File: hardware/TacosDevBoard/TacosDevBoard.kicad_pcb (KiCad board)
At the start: 2 copper layers, 63.6 x 108.1 mm, 12 parts, among them IC2_COMM1 Conn_01x08_Socket, J1 Conn_01x08_Socket, J2 Conn_01x08_Socket, J3 Conn_01x08_Socket, J4 Conn_01x08_Socket, J5 Conn_01x08_Socket, J6 Micro_SD_Card_Det2, J7 Conn_02x17_Counter_Clockwise, J9 Conn_01x10_Pin

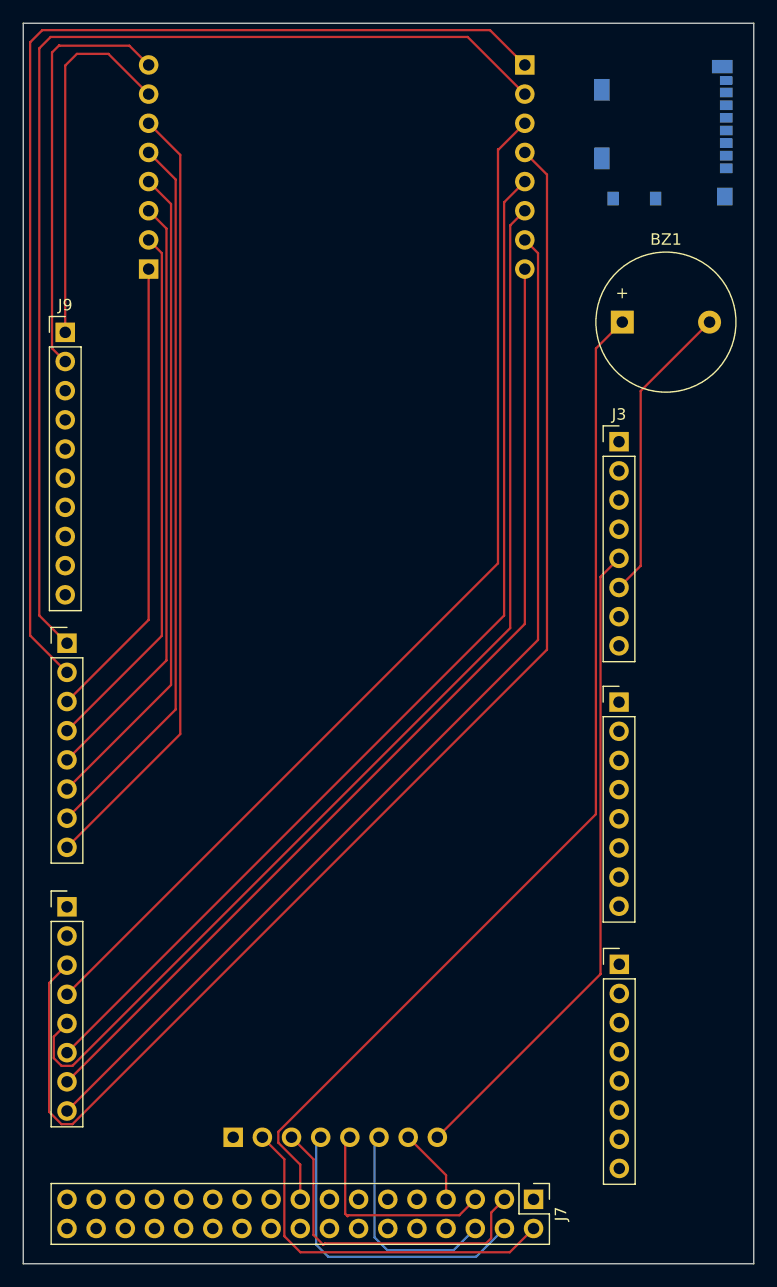
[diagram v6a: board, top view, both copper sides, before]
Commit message: added sd card to dev board
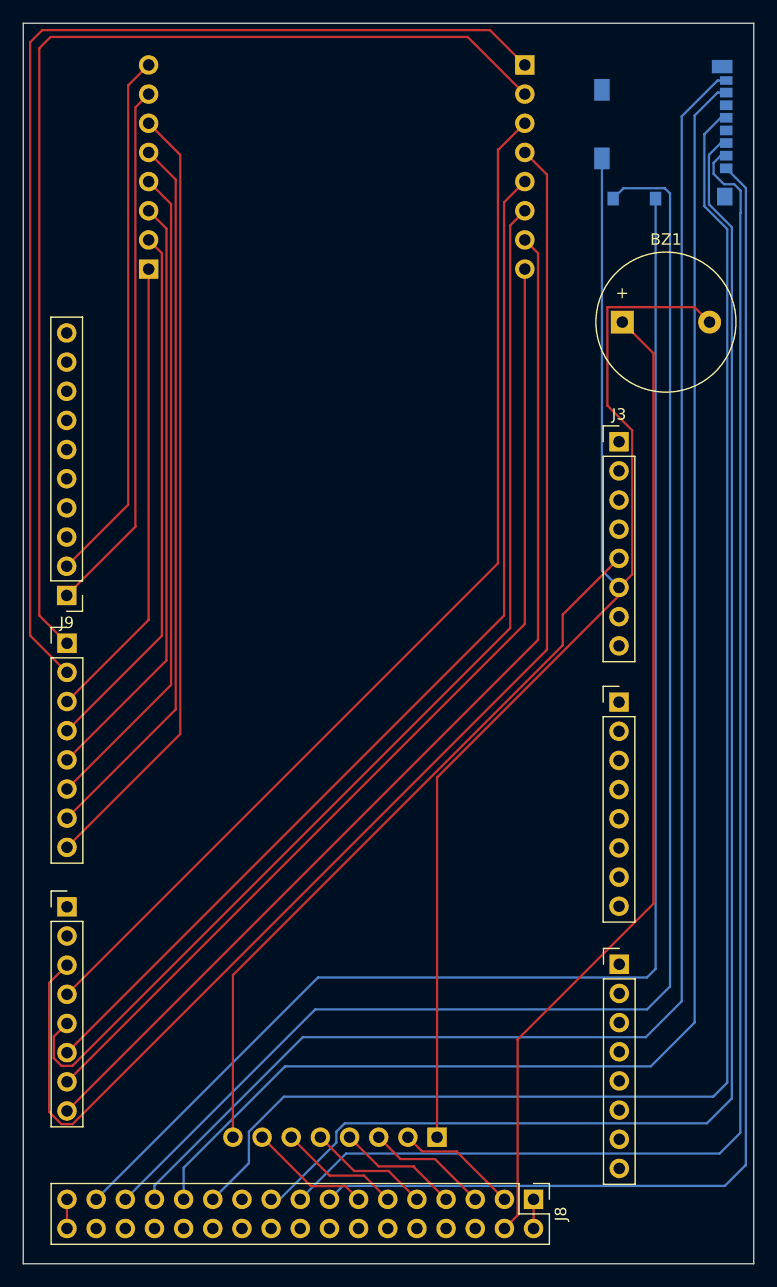
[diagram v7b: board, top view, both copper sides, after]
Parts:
- removed J7: Conn_02x17_Counter_Clockwise, Connector_PinHeader_2.54mm:PinHeader_2x17_P2.54mm_Vertical
- added J8: Conn_02x17_Odd_Even, Connector_PinHeader_2.54mm:PinHeader_2x17_P2.54mm_Vertical, F.Cu at (153.7, 136.9)
- moved J9 22.9 mm to (113.0, 84.3), turned to 180 degrees
- moved SELECT1 17.8 mm to (145.3, 131.5), turned to 90 degrees
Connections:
- J3 pad 4: +3.3V -> VDD
- J3 pad 7: GND -> VSS
- J6 pad 1: Net-(J6-DAT2) -> SD_DAT2
- J6 pad 10: Net-(J6-DET_A) -> SD_DET_A
- J6 pad 11: unconnected-(J6-SHIELD-Pad11) -> GND
- J6 pad 2: Net-(J6-DAT3/CD) -> SD_DAT3/CD
- J6 pad 3: Net-(J6-CMD) -> SD_CMD
- J6 pad 4: Net-(J6-VDD) -> VDD
- J6 pad 5: Net-(J6-CLK) -> SD_CLK
- J6 pad 6: Net-(J6-VSS) -> VSS
- J6 pad 7: Net-(J6-DAT0) -> SD_DAT0
- J6 pad 8: Net-(J6-DAT1) -> SD_DAT1
- J6 pad 9: Net-(J6-DET_B) -> SD_DET_B
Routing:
- net SD_CLK: track 0.00 -> 136.6 mm
- net SD_DAT1: track 0.00 -> 136.0 mm
- net SD_DAT0: track 0.00 -> 135.1 mm
- net SD_DET_A: track 0.00 -> 129.7 mm
- net SD_CMD: track 0.00 -> 129.3 mm
- net SD_DAT3/CD: track 0.00 -> 128.1 mm
- net SD_DAT2: track 0.00 -> 125.0 mm
- net SD_DET_B: track 0.00 -> 124.1 mm
- net GND: track 26.4 -> 130.2 mm
- net D22: track 32.6 -> 10.7 mm
- net D24: track 29.2 -> 10.6 mm
- net D26: track 27.4 -> 10.7 mm
- net ~D8: track 32.4 -> 46.6 mm
- net +5V: track 57.0 -> 66.9 mm
- net ~D9: track 36.8 -> 46.6 mm
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
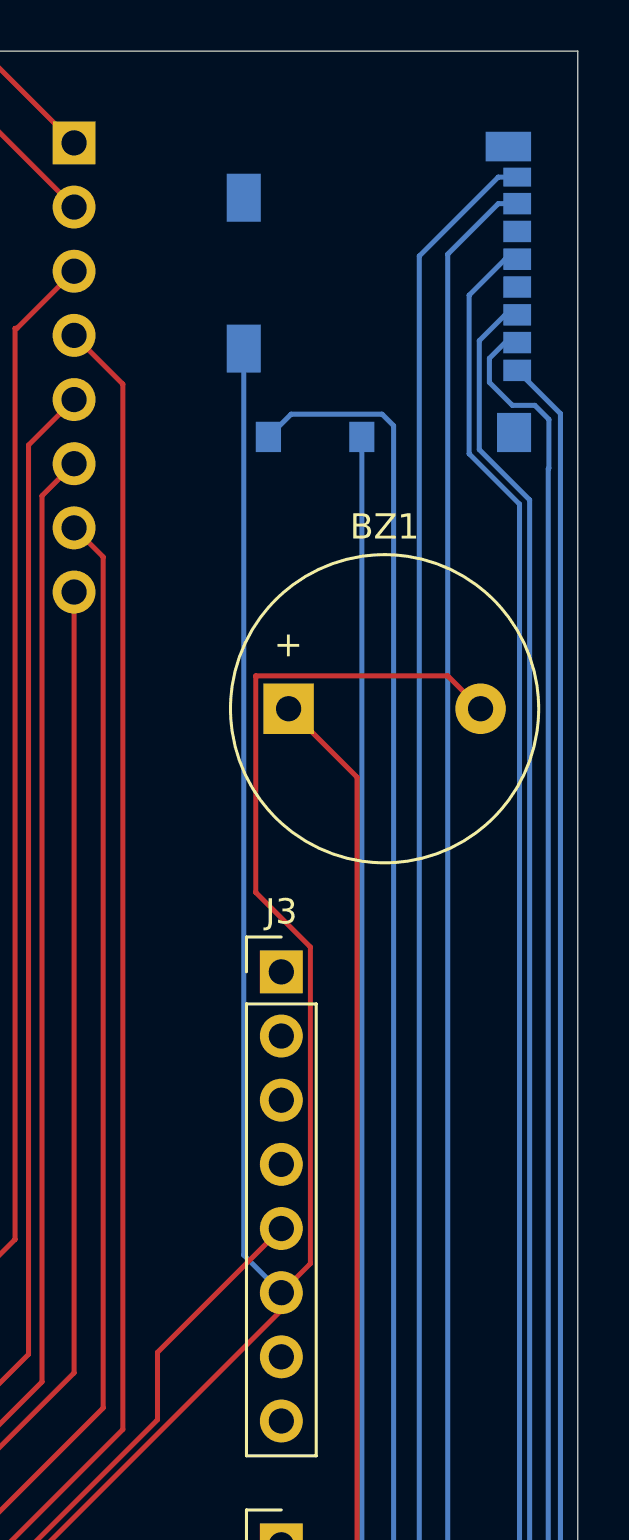
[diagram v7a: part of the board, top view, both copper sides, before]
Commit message: added power for sd
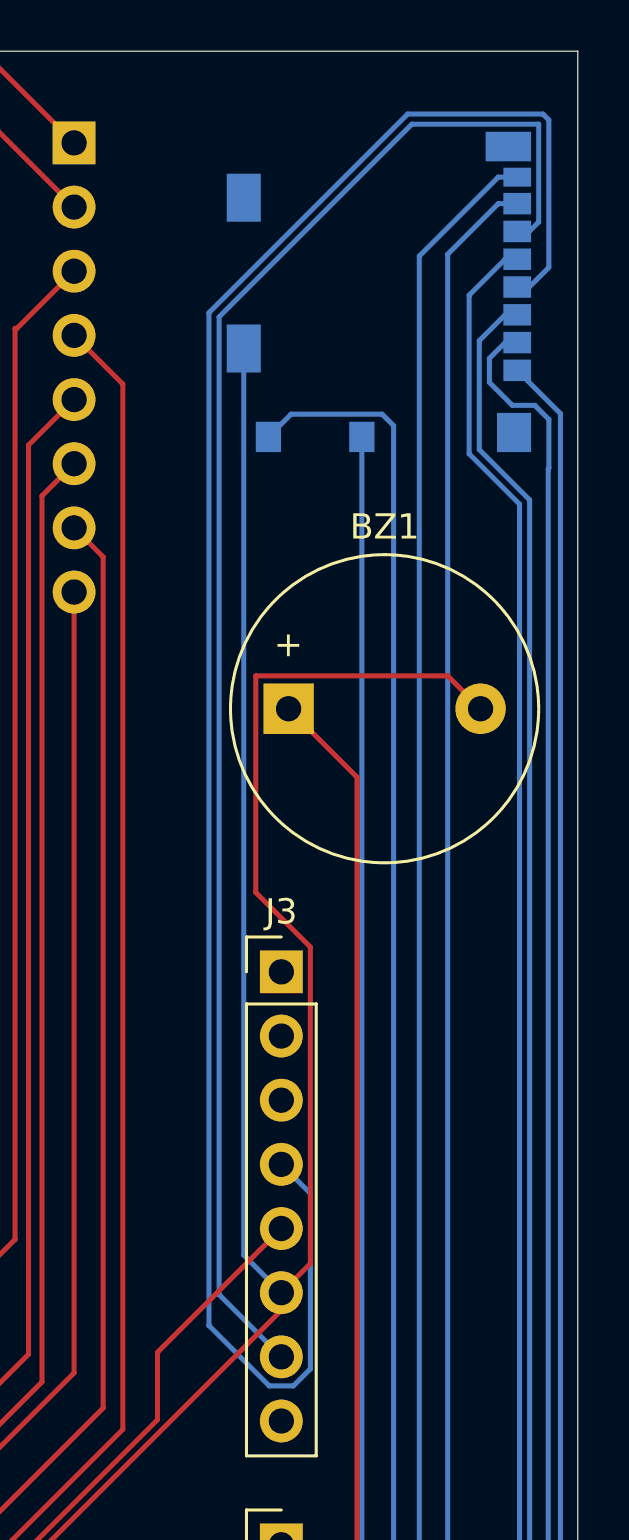
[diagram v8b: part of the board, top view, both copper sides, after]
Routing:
- net VDD: track 0.00 -> 78.2 mm
- net VSS: track 0.00 -> 62.9 mm
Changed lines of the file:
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@@
 		(net 70)
+	)
+	(segment
+		(start 171.702 37.1929)
+		(end 171.4671 36.958)
+		(width 0.2)
+		(layer "B.Cu")
+		(net 78)
+	)
+	(segment
+		(start 170.927 43.805)
+		(end 171.702 43.03)
+		(width 0.2)
+		(layer "B.Cu")
+		(net 78)
+	)
+	(segment
+		(start 162.2632 86.63356)
+		(end 162.2632 79.6878)
+		(width 0.2)
+		(layer "B.Cu")
+		(net 78)
+	)
+	(segment
+		(start 162.2632 79.6878)
+		(end 161.1122 78.5368)
+		(width 0.2)
+		(layer "B.Cu")
+		(net 78)
+	)
+	(segment
+		(start 166.1129 36.958)
+		(end 158.248 44.8229)
+		(width 0.2)
+		(layer "B.Cu")
+		(net 78)
+	)
+	(segment
+		(start 171.702 43.03)
+		(end 171.702 37.1929)
+		(width 0.2)
+		(layer "B.Cu")
+		(net 78)
+	)
+	(segment
+		(start 161.58896 87.3078)
+		(end 162.2632 86.63356)
+		(width 0.2)
+		(layer "B.Cu")
+		(net 78)
+	)
+	(segment
+		(start 158.248 84.92036)
+		(end 160.63544 87.3078)
+		(width 0.2)
+		(layer "B.Cu")
+		(net 78)
+	)
+	(segment
+		(start 170.45 43.805)
+		(end 170.927 43.805)
+		(width 0.2)
+		(layer "B.Cu")
+		(net 78)
+	)
+	(segment
+		(start 160.63544 87.3078)
+		(end 161.58896 87.3078)
+		(width 0.2)
+		(layer "B.Cu")
+		(net 78)
+	)
+	(segment
+		(start 158.248 44.8229)
+		(end 158.248 84.92036)
+		(width 0.2)
+		(layer "B.Cu")
+		(net 78)
+	)
+	(segment
+		(start 171.4671 36.958)
+		(end 166.1129 36.958)
+		(width 0.2)
+		(layer "B.Cu")
+		(net 78)
+	)
+	(segment
+		(start 158.649 83.6936)
+		(end 161.1122 86.1568)
+		(width 0.2)
+		(layer "B.Cu")
+		(net 79)
+	)
+	(segment
+		(start 171.301 37.359)
+		(end 166.279 37.359)
+		(width 0.2)
+		(layer "B.Cu")
+		(net 79)
+	)
+	(segment
+		(start 170.45 41.605)
+		(end 170.927 41.605)
+		(width 0.2)
+		(layer "B.Cu")
+		(net 79)
+	)
+	(segment
+		(start 158.649 44.989)
+		(end 158.649 83.6936)
+		(width 0.2)
+		(layer "B.Cu")
+		(net 79)
+	)
+	(segment
+		(start 166.279 37.359)
+		(end 158.649 44.989)
+		(width 0.2)
+		(layer "B.Cu")
+		(net 79)
+	)
+	(segment
+		(start 171.301 41.231)
+		(end 171.301 37.359)
+		(width 0.2)
+		(layer "B.Cu")
+		(net 79)
+	)
+	(segment
+		(start 170.927 41.605)
+		(end 171.301 41.231)
+		(width 0.2)
+		(layer "B.Cu")
+		(net 79)
 	)
 	(embedded_fonts no)
